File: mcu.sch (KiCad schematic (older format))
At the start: 17 parts, among them U201 STM32F072C8Tx, Y201 8MHz

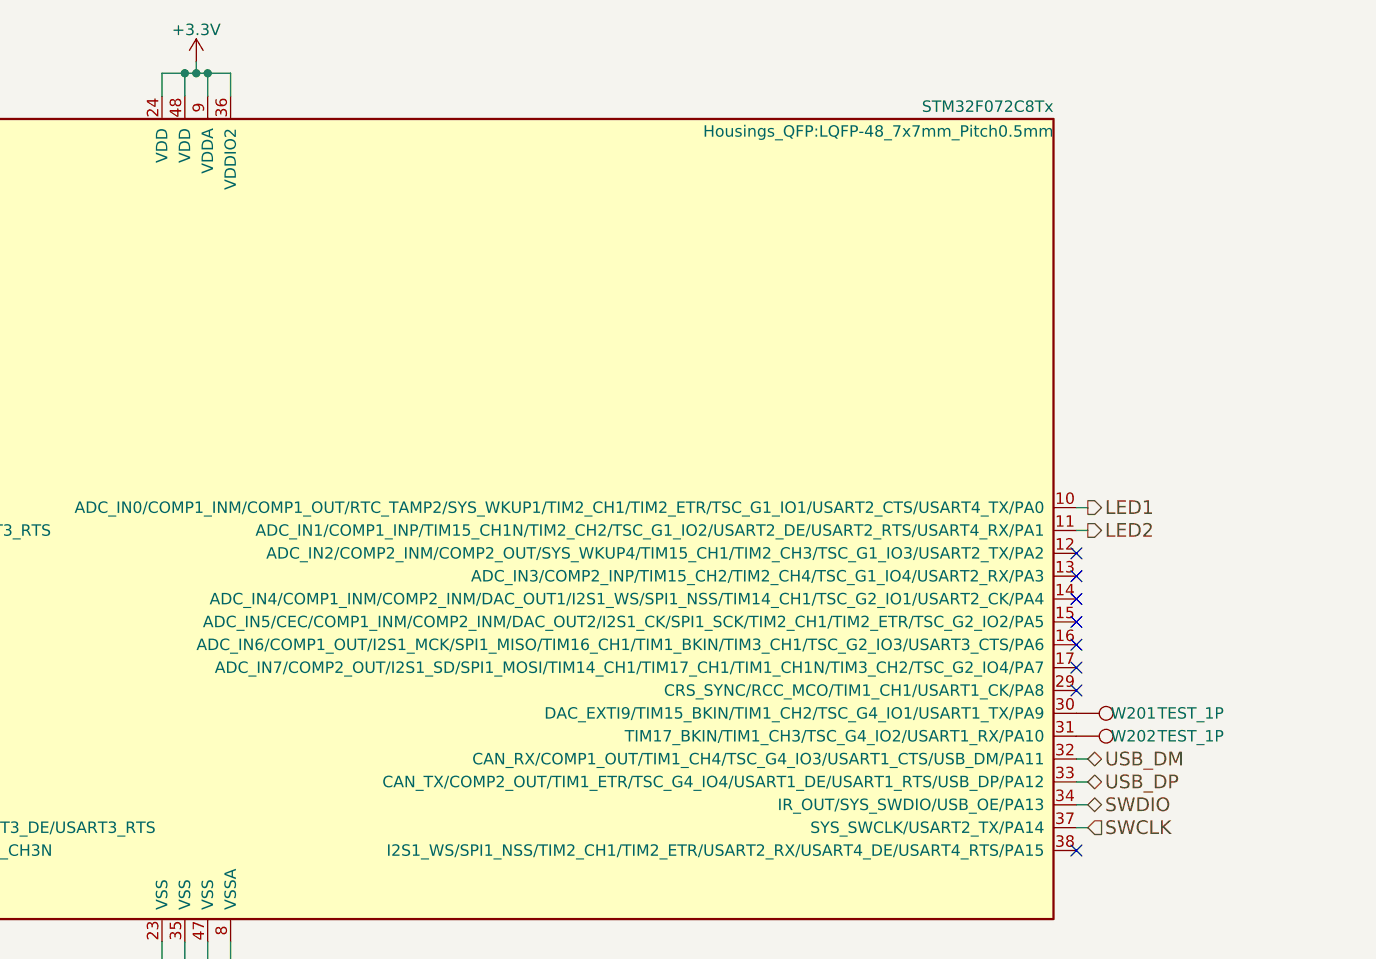
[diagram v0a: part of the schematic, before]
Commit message: add missing usb data line resistors
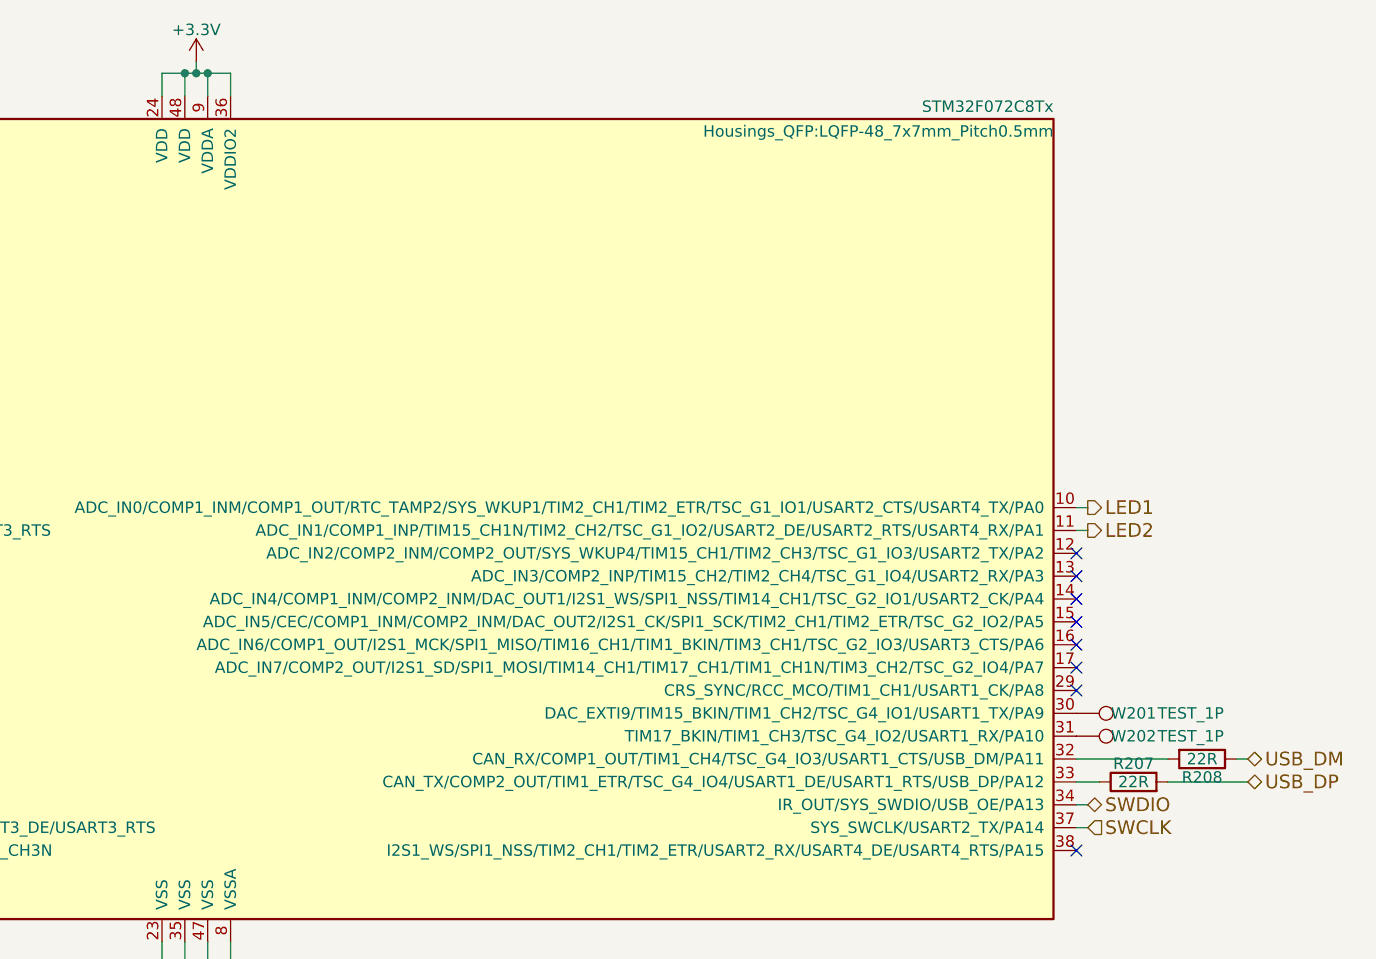
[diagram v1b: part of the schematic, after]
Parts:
- added R207, R208: 22R, Resistors_SMD:R_0603, symbol R
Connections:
- net USB_DM: now also R208.1; no longer U201.32 (CAN_RX/COMP1_OUT/TIM1_CH4/TSC_G4_IO3/USART1_CTS/USB_DM/PA11)
- net USB_DP: now also R207.2; no longer U201.33 (CAN_TX/COMP2_OUT/TIM1_ETR/TSC_G4_IO4/USART1_DE/USART1_RTS/USB_DP/PA12)
- new net: R208.2, U201.32 (CAN_RX/COMP1_OUT/TIM1_CH4/TSC_G4_IO3/USART1_CTS/USB_DM/PA11)
- new net: R207.1, U201.33 (CAN_TX/COMP2_OUT/TIM1_ETR/TSC_G4_IO4/USART1_DE/USART1_RTS/USB_DP/PA12)
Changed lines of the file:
@@
 $EndDescr
 $Comp
-L GND #PWR01
+L GND #PWR217
 U 1 1 56F3B243
 P 5750 6000
-F 0 "#PWR01" H 5750 5750 50  0001 C CNN
+F 0 "#PWR217" H 5750 5750 50  0001 C CNN
 F 1 "GND" H 5750 5850 50  0000 C CNN
 F 2 "" H 5750 6000 50  0000 C CNN
@@
 NRST
 $Comp
-L +3V3 #PWR02
+L +3V3 #PWR209
 U 1 1 56F3BCC8
 P 2000 2900
-F 0 "#PWR02" H 2000 2750 50  0001 C CNN
+F 0 "#PWR209" H 2000 2750 50  0001 C CNN
 F 1 "+3V3" H 2000 3040 50  0000 C CNN
 F 2 "" H 2000 2900 50  0000 C CNN
@@
 Text HLabel 9650 5100 2    60   BiDi ~ 0
 SWDIO
-Text HLabel 9650 5000 2    60   BiDi ~ 0
+Text HLabel 10350 5000 2    60   BiDi ~ 0
 USB_DP
-Text HLabel 9650 4900 2    60   BiDi ~ 0
+Text HLabel 10350 4900 2    60   BiDi ~ 0
 USB_DM
 Text HLabel 1950 4600 0    60   Input ~ 0
@@
 $EndComp
 $Comp
-L +3.3V #PWR03
+L +3.3V #PWR202
 U 1 1 56F50A4B
 P 1150 4300
-F 0 "#PWR03" H 1150 4150 50  0001 C CNN
+F 0 "#PWR202" H 1150 4150 50  0001 C CNN
 F 1 "+3.3V" H 1150 4440 50  0000 C CNN
 F 2 "" H 1150 4300 50  0000 C CNN
@@
 $EndComp
 $Comp
-L +3.3V #PWR04
+L +3.3V #PWR203
 U 1 1 56F51029
 P 1450 2600
-F 0 "#PWR04" H 1450 2450 50  0001 C CNN
+F 0 "#PWR203" H 1450 2450 50  0001 C CNN
 F 1 "+3.3V" H 1450 2740 50  0000 C CNN
 F 2 "" H 1450 2600 50  0000 C CNN
@@
 $EndComp
 $Comp
-L GND #PWR05
+L GND #PWR204
 U 1 1 56F5105F
 P 1450 2800
-F 0 "#PWR05" H 1450 2550 50  0001 C CNN
+F 0 "#PWR204" H 1450 2550 50  0001 C CNN
 F 1 "GND" H 1450 2650 50  0000 C CNN
 F 2 "" H 1450 2800 50  0000 C CNN
@@
 $EndComp
 $Comp
-L GND #PWR06
+L GND #PWR201
 U 1 1 56F51B19
 P 900 3150
-F 0 "#PWR06" H 900 2900 50  0001 C CNN
+F 0 "#PWR201" H 900 2900 50  0001 C CNN
 F 1 "GND" H 900 3000 50  0000 C CNN
 F 2 "" H 900 3150 50  0000 C CNN
@@
 $EndComp
 $Comp
-L +3.3V #PWR07
+L +3.3V #PWR216
 U 1 1 56F53AB0
 P 5750 1850
-F 0 "#PWR07" H 5750 1700 50  0001 C CNN
+F 0 "#PWR216" H 5750 1700 50  0001 C CNN
 F 1 "+3.3V" H 5750 1990 50  0000 C CNN
 F 2 "" H 5750 1850 50  0000 C CNN
@@
 $EndComp
 $Comp
-L +3.3V #PWR08
+L +3.3V #PWR212
 U 1 1 56F53F33
 P 2500 6750
-F 0 "#PWR08" H 2500 6600 50  0001 C CNN
+F 0 "#PWR212" H 2500 6600 50  0001 C CNN
 F 1 "+3.3V" H 2500 6890 50  0000 C CNN
 F 2 "" H 2500 6750 50  0000 C CNN
@@
 $EndComp
 $Comp
-L GND #PWR09
+L GND #PWR213
 U 1 1 56F53F61
 P 2500 6950
-F 0 "#PWR09" H 2500 6700 50  0001 C CNN
+F 0 "#PWR213" H 2500 6700 50  0001 C CNN
 F 1 "GND" H 2500 6800 50  0000 C CNN
 F 2 "" H 2500 6950 50  0000 C CNN
@@
 $EndComp
 $Comp
-L +3.3V #PWR010
+L +3.3V #PWR210
 U 1 1 56F54055
 P 2200 6750
-F 0 "#PWR010" H 2200 6600 50  0001 C CNN
+F 0 "#PWR210" H 2200 6600 50  0001 C CNN
 F 1 "+3.3V" H 2200 6890 50  0000 C CNN
 F 2 "" H 2200 6750 50  0000 C CNN
@@
 $EndComp
 $Comp
-L GND #PWR011
+L GND #PWR211
 U 1 1 56F5405B
 P 2200 6950
-F 0 "#PWR011" H 2200 6700 50  0001 C CNN
+F 0 "#PWR211" H 2200 6700 50  0001 C CNN
 F 1 "GND" H 2200 6800 50  0000 C CNN
 F 2 "" H 2200 6950 50  0000 C CNN
@@
 $EndComp
 $Comp
-L +3.3V #PWR012
+L +3.3V #PWR207
 U 1 1 56F54100
 P 1900 6750
-F 0 "#PWR012" H 1900 6600 50  0001 C CNN
+F 0 "#PWR207" H 1900 6600 50  0001 C CNN
 F 1 "+3.3V" H 1900 6890 50  0000 C CNN
 F 2 "" H 1900 6750 50  0000 C CNN
@@
 $EndComp
 $Comp
-L GND #PWR013
+L GND #PWR208
 U 1 1 56F54106
 P 1900 6950
-F 0 "#PWR013" H 1900 6700 50  0001 C CNN
+F 0 "#PWR208" H 1900 6700 50  0001 C CNN
 F 1 "GND" H 1900 6800 50  0000 C CNN
 F 2 "" H 1900 6950 50  0000 C CNN
@@
 $EndComp
 $Comp
-L +3.3V #PWR014
+L +3.3V #PWR205
 U 1 1 56F54112
 P 1600 6750
-F 0 "#PWR014" H 1600 6600 50  0001 C CNN
+F 0 "#PWR205" H 1600 6600 50  0001 C CNN
 F 1 "+3.3V" H 1600 6890 50  0000 C CNN
 F 2 "" H 1600 6750 50  0000 C CNN
@@
 $EndComp
 $Comp
-L GND #PWR015
+L GND #PWR206
 U 1 1 56F54118
 P 1600 6950
-F 0 "#PWR015" H 1600 6700 50  0001 C CNN
+F 0 "#PWR206" H 1600 6700 50  0001 C CNN
 F 1 "GND" H 1600 6800 50  0000 C CNN
 F 2 "" H 1600 6950 50  0000 C CNN
@@
 $EndComp
 $Comp
-L +3.3V #PWR016
+L +3.3V #PWR214
 U 1 1 56F5425C
 P 2950 6750
-F 0 "#PWR016" H 2950 6600 50  0001 C CNN
+F 0 "#PWR214" H 2950 6600 50  0001 C CNN
 F 1 "+3.3V" H 2950 6890 50  0000 C CNN
 F 2 "" H 2950 6750 50  0000 C CNN
@@
 $EndComp
 $Comp
-L GND #PWR017
+L GND #PWR215
 U 1 1 56F54262
 P 2950 6950
-F 0 "#PWR017" H 2950 6700 50  0001 C CNN
+F 0 "#PWR215" H 2950 6700 50  0001 C CNN
 F 1 "GND" H 2950 6800 50  0000 C CNN
 F 2 "" H 2950 6950 50  0000 C CNN
@@
 	1900 3200 2000 3200
 Wire Wire Line
-	5900 2000 5900 1900
-Wire Wire Line
-	5900 1900 5600 1900
+	5900 1900 5900 2000
+Wire Wire Line
+	5600 1900 5900 1900
 Wire Wire Line
 	5600 1900 5600 2000
@@
 	9600 5100 9650 5100
 Wire Wire Line
-	9600 5000 9650 5000
-Wire Wire Line
-	9600 4900 9650 4900
-Wire Wire Line
 	9600 3900 9650 3900
 Wire Wire Line
@@
 	2000 3400 1900 3400
 NoConn ~ 2000 4300
+$Comp
+L R R208
+U 1 1 56FAF8BC
+P 10150 4900
+F 0 "R208" V 10230 4900 50  0000 C CNN
+F 1 "22R" V 10150 4900 50  0000 C CNN
+F 2 "Resistors_SMD:R_0603" V 10080 4900 50  0001 C CNN
+F 3 "" H 10150 4900 50  0000 C CNN
+	1    10150 4900
+	0    1    1    0
+$EndComp
+$Comp
+L R R207
+U 1 1 56FAF9D1
+P 9850 5000
+F 0 "R207" V 9930 5000 50  0000 C CNN
+F 1 "22R" V 9850 5000 50  0000 C CNN
+F 2 "Resistors_SMD:R_0603" V 9780 5000 50  0001 C CNN
+F 3 "" H 9850 5000 50  0000 C CNN
+	1    9850 5000
+	0    -1   -1   0
+$EndComp
+Wire Wire Line
+	9700 5000 9600 5000
+Wire Wire Line
+	10300 4900 10350 4900
+Wire Wire Line
+	9600 4900 10000 4900
+Wire Wire Line
+	10000 5000 10350 5000
 $EndSCHEMATC

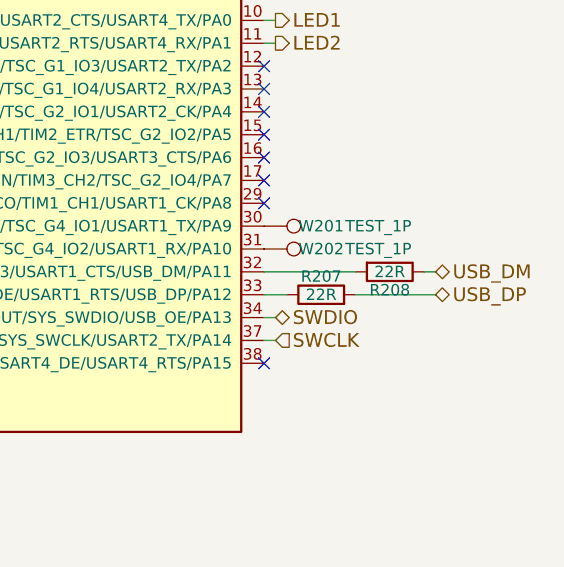
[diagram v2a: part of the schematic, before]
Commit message: remove unneeded parts
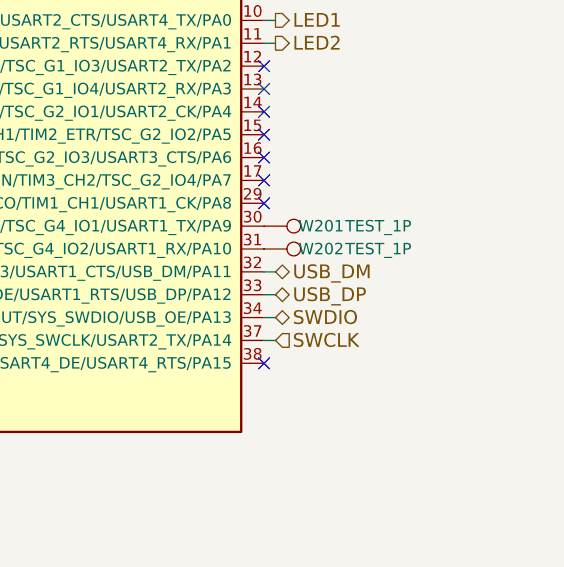
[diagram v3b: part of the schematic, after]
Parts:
- removed R207, R208: 22R, Resistors_SMD:R_0603, symbol R
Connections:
- net USB_DM: now also U201.32 (CAN_RX/COMP1_OUT/TIM1_CH4/TSC_G4_IO3/USART1_CTS/USB_DM/PA11)
- net USB_DP: now also U201.33 (CAN_TX/COMP2_OUT/TIM1_ETR/TSC_G4_IO4/USART1_DE/USART1_RTS/USB_DP/PA12)
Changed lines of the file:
@@
 Text HLabel 9650 5100 2    60   BiDi ~ 0
 SWDIO
-Text HLabel 10350 5000 2    60   BiDi ~ 0
+Text HLabel 9650 5000 2    60   BiDi ~ 0
 USB_DP
-Text HLabel 10350 4900 2    60   BiDi ~ 0
+Text HLabel 9650 4900 2    60   BiDi ~ 0
 USB_DM
 Text HLabel 1950 4600 0    60   Input ~ 0
@@
 	2000 3400 1900 3400
 NoConn ~ 2000 4300
-$Comp
-L R R208
-U 1 1 56FAF8BC
-P 10150 4900
-F 0 "R208" V 10230 4900 50  0000 C CNN
-F 1 "22R" V 10150 4900 50  0000 C CNN
-F 2 "Resistors_SMD:R_0603" V 10080 4900 50  0001 C CNN
-F 3 "" H 10150 4900 50  0000 C CNN
-	1    10150 4900
-	0    1    1    0
-$EndComp
-$Comp
-L R R207
-U 1 1 56FAF9D1
-P 9850 5000
-F 0 "R207" V 9930 5000 50  0000 C CNN
-F 1 "22R" V 9850 5000 50  0000 C CNN
-F 2 "Resistors_SMD:R_0603" V 9780 5000 50  0001 C CNN
-F 3 "" H 9850 5000 50  0000 C CNN
-	1    9850 5000
-	0    -1   -1   0
-$EndComp
-Wire Wire Line
-	9700 5000 9600 5000
-Wire Wire Line
-	10300 4900 10350 4900
-Wire Wire Line
-	9600 4900 10000 4900
-Wire Wire Line
-	10000 5000 10350 5000
+Wire Wire Line
+	9650 5000 9600 5000
+Wire Wire Line
+	9650 4900 9600 4900
 $EndSCHEMATC

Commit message: add testpoints, reset line cap
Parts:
- added C208: 100nF, Capacitors_SMD:C_0603, symbol C_Small
- added W203, W204, W205, W206, W207, W208: TEST_1P, Measurement_Points:Measurement_Point_Round-SMD-Pad_Small, symbol TEST_1P
- R203: footprint Resistors_SMD:R_0603 -> Resistors_SMD:R_0805
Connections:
- net GND: now also R204.1, C208.2; no longer R204.2
- net NRST: now also C208.1
- net at U201.25 (PB12/I2S2_WS/SPI2_NSS/TIM15_BKIN/TIM1_BKIN/TSC_G6_IO2/USART3_CK): now also W205.1
- net at U201.26 (PB13/I2C2_SCL/I2S2_CK/SPI2_SCK/TIM1_CH1N/TSC_G6_IO3/USART3_CTS): now also W206.1
- net at U201.27 (PB14/I2C2_SDA/I2S2_MCK/SPI2_MISO/TIM15_CH1/TIM1_CH2N/TSC_G6_IO4/USART3_DE/USART3_RTS): now also W207.1
- net at U201.28 (PB15/I2S2_SD/RTC_REFIN/SPI2_MOSI/SYS_WKUP7/TIM15_CH1N/TIM15_CH2/TIM1_CH3N): now also W208.1
- net at R201.2, U201.42 (PB6/I2C1_SCL/TIM16_CH1N/TSC_G5_IO3/USART1_TX): now also W203.1
- net at R202.1, U201.43 (PB7/I2C1_SDA/TIM17_CH1N/TSC_G5_IO4/USART1_RX/USART4_CTS): now also W204.1
- net BOOT0: now reaches R203.2, U201.44 (BOOT0)
- net BOOT0: now also R204.2; no longer R204.1
- no-connect marks 22 -> 18
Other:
- moved on the sheet: R201, R202, R203, R204

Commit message: candleLight v1.2
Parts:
- removed R205, R206: 0R, Resistors_SMD:R_0603, symbol R
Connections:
- net at U201.5 (PF0/CRS_SYNC/RCC_OSC_IN): now also C201.2, Y201.1
- net at U201.6 (PF1/RCC_OSC_OUT): now also C202.2, Y201.2
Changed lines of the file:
@@
 	1    0    0    -1
-$EndComp
-$Comp
-L R R205
-U 1 1 56F472B8
-P 1750 3100
-F 0 "R205" V 1830 3100 50  0000 C CNN
-F 1 "0R" V 1750 3100 50  0000 C CNN
-F 2 "Resistors_SMD:R_0603" V 1680 3100 50  0001 C CNN
-F 3 "" H 1750 3100 50  0000 C CNN
-	1    1750 3100
-	0    -1   -1   0
-$EndComp
-$Comp
-L R R206
-U 1 1 56F4730D
-P 1750 3200
-F 0 "R206" V 1830 3200 50  0000 C CNN
-F 1 "0R" V 1750 3200 50  0000 C CNN
-F 2 "Resistors_SMD:R_0603" V 1680 3200 50  0001 C CNN
-F 3 "" H 1750 3200 50  0000 C CNN
-	1    1750 3200
-	0    1    1    0
 $EndComp
 Text HLabel 9650 5200 2    60   Input ~ 0
@@
 	5700 5700 5700 5900
 Wire Wire Line
-	5600 5900 5900 5900
+	5600 5900 5700 5900
+Wire Wire Line
+	5700 5900 5750 5900
+Wire Wire Line
+	5750 5900 5800 5900
+Wire Wire Line
+	5800 5900 5900 5900
 Wire Wire Line
 	5800 5900 5800 5700
@@
 Connection ~ 5800 5900
 Wire Wire Line
-	1300 4400 2000 4400
-Wire Wire Line
-	1300 4500 2000 4500
-Wire Wire Line
-	950  4300 950  4500
+	1300 4400 1400 4400
+Wire Wire Line
+	1400 4400 2000 4400
+Wire Wire Line
+	1300 4500 1400 4500
+Wire Wire Line
+	1400 4500 2000 4500
+Wire Wire Line
+	950  4300 950  4400
+Wire Wire Line
+	950  4400 950  4500
 Wire Wire Line
 	950  4400 1000 4400
@@
 Connection ~ 950  4400
 Wire Wire Line
-	1600 3100 1500 3100
-Wire Wire Line
-	1500 3100 1500 3050
-Wire Wire Line
-	1500 3050 1200 3050
-Wire Wire Line
-	1600 3200 1500 3200
-Wire Wire Line
-	1500 3200 1500 3250
-Wire Wire Line
-	1500 3250 1200 3250
+	1650 3100 2000 3100
+Wire Wire Line
+	1650 3100 1650 3050
+Wire Wire Line
+	1650 3050 1350 3050
+Wire Wire Line
+	1350 3050 1200 3050
+Wire Wire Line
+	1650 3200 2000 3200
+Wire Wire Line
+	1650 3200 1650 3250
+Wire Wire Line
+	1650 3250 1350 3250
+Wire Wire Line
+	1350 3250 1200 3250
 Connection ~ 1350 3050
 Connection ~ 1350 3250
 Wire Wire Line
-	1900 3100 2000 3100
-Wire Wire Line
-	1900 3200 2000 3200
-Wire Wire Line
 	5900 1900 5900 2000
 Wire Wire Line
-	5600 1900 5900 1900
+	5600 1900 5700 1900
+Wire Wire Line
+	5700 1900 5750 1900
+Wire Wire Line
+	5750 1900 5800 1900
+Wire Wire Line
+	5800 1900 5900 1900
 Wire Wire Line
 	5600 1900 5600 2000
@@
 	1650 2700 2000 2700
 Wire Wire Line
-	3900 6650 3900 6750
+	3900 6650 3900 6700
+Wire Wire Line
+	3900 6700 3900 6750
 Text Label 4250 6700 2    60   ~ 0
 BOOT0
@@
 $EndComp
 Wire Wire Line
-	1150 2500 2000 2500
+	1150 2500 1350 2500
+Wire Wire Line
+	1350 2500 2000 2500
 Wire Wire Line
 	1350 2500 1350 2550
@@
 	850  3150 900  3150
 Wire Wire Line
-	900  3050 900  3250
+	900  3050 900  3150
+Wire Wire Line
+	900  3150 900  3250
 Wire Wire Line
 	900  3050 1000 3050
